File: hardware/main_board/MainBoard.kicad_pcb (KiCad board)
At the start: 2 copper layers, 68 parts, among them J1 5V In, J11 Conn_01x01, J12 GREEN, J13 Conn_01x05, J14 Conn_01x04, J2 9V In, J3 Conn_01x08, J4 Conn_01x08, J5 Conn_01x08, J6 Conn_01x08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

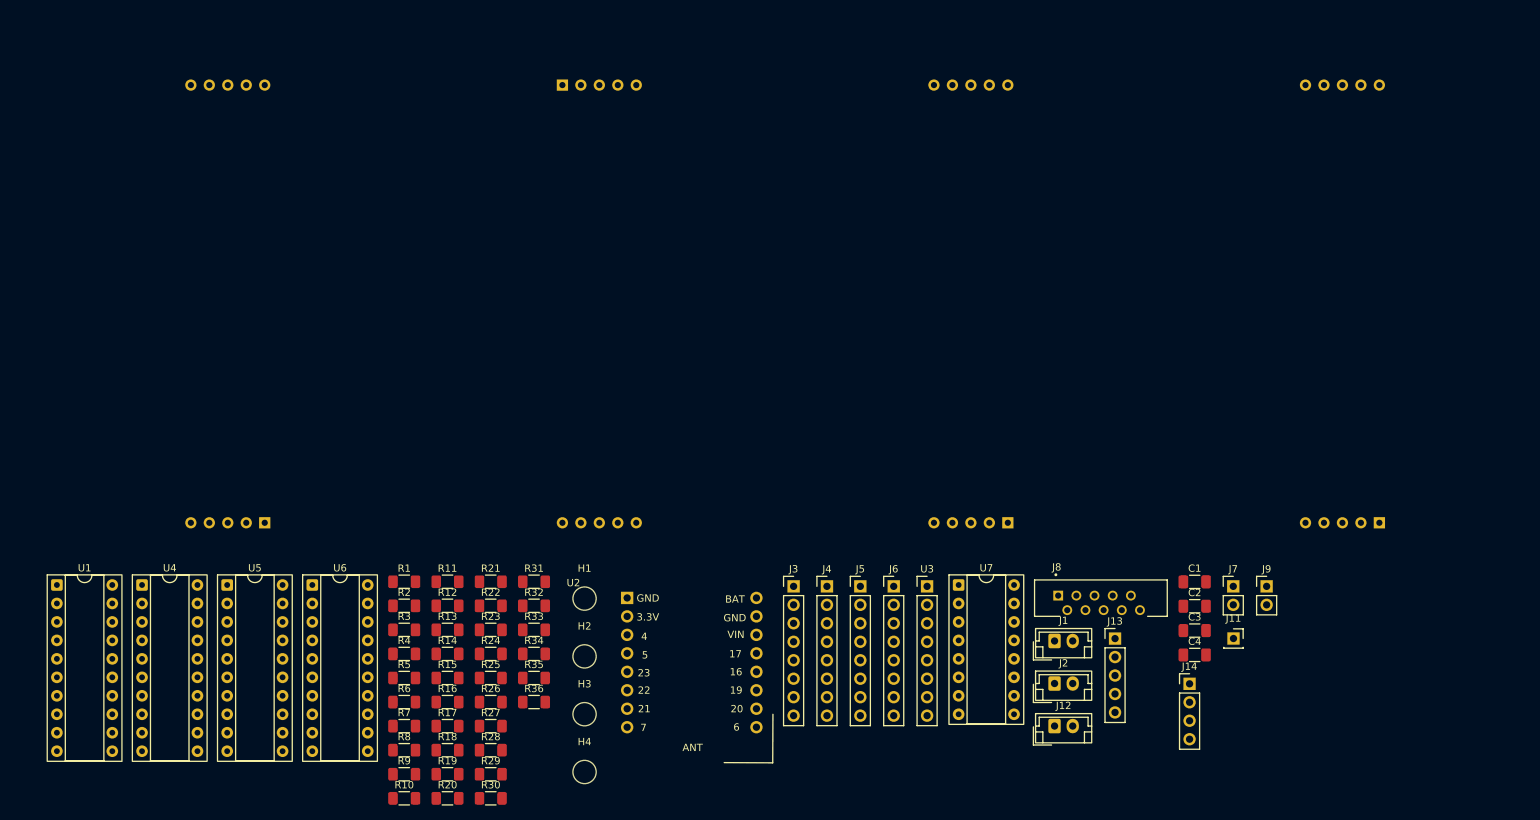
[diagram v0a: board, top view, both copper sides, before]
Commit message: Started 2 layer mainboard, switching to 4 layer
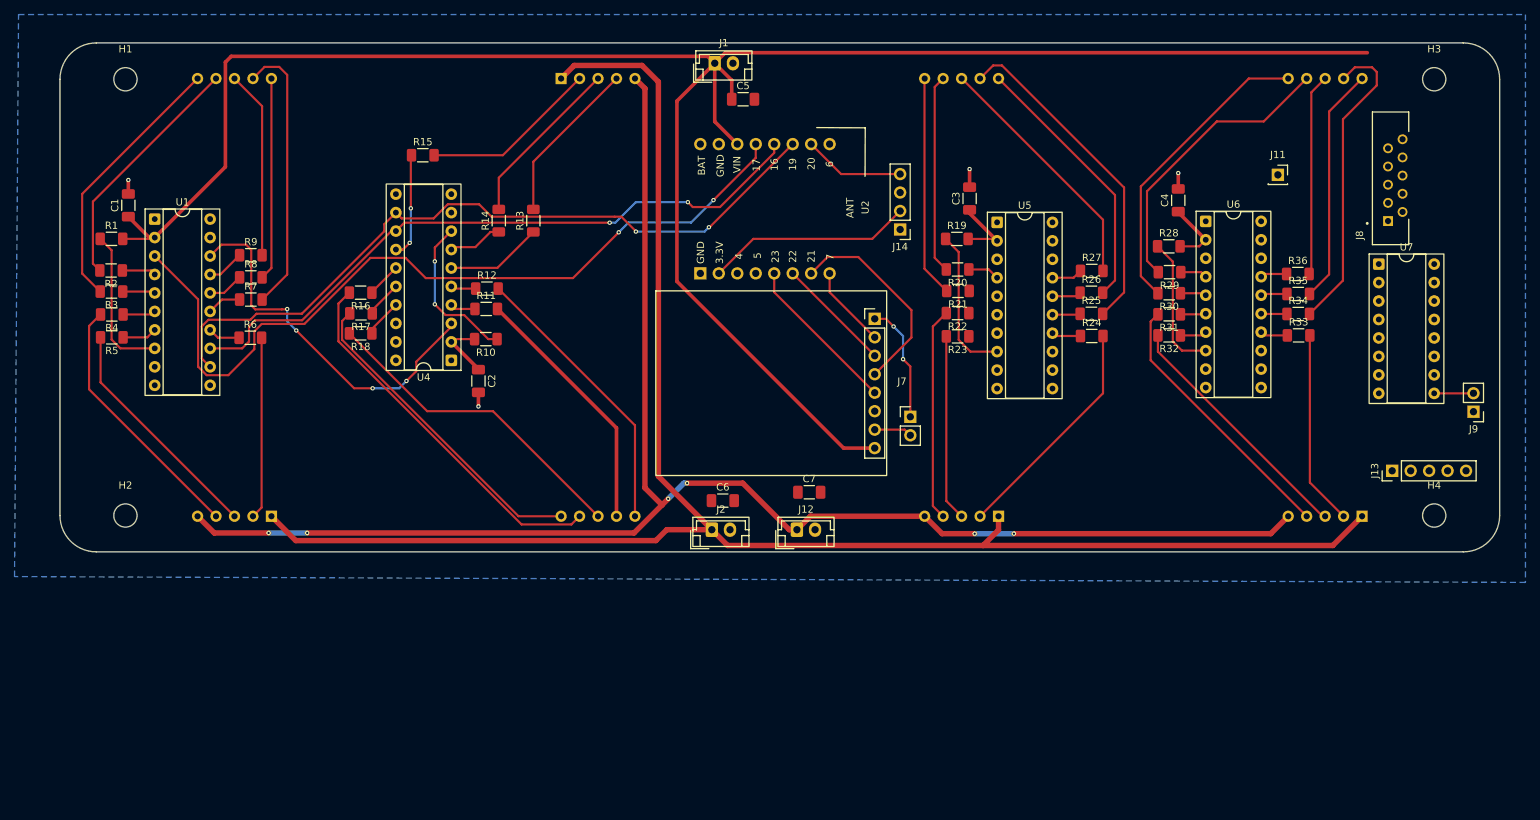
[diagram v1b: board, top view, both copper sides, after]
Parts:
- removed J3, J4, J5, J6: Conn_01x08, Connector_PinHeader_2.54mm:PinHeader_1x08_P2.54mm_Vertical
- added C5: C, Capacitor_SMD:C_1206_3216Metric_Pad1.33x1.80mm_HandSolder, F.Cu at (144.9, 32.8)
- added C6: C, Capacitor_SMD:C_1206_3216Metric_Pad1.33x1.80mm_HandSolder, F.Cu at (142.2, 88.0)
- added C7: C, Capacitor_SMD:C_1206_3216Metric_Pad1.33x1.80mm_HandSolder, F.Cu at (154.1, 86.8)
- U3: footprint Connector_PinHeader_2.54mm:PinHeader_1x08_P2.54mm_Vertical -> GregFootprints:SD Card
- moved C1 155.5 mm to (60.4, 47.3), turned to 90 degrees
- moved H3 145.9 mm to (240.0, 30.0)
- moved U6 132.7 mm to (208.6, 49.5)
- moved H4 122.1 mm to (240.0, 90.0)
- moved R36 120.4 mm to (221.2, 56.8)
- moved R35 117.6 mm to (221.3, 59.5)
- moved U5 117.0 mm to (179.9, 49.7)
- moved R30 116.3 mm to (203.6, 59.4), turned to 180 degrees
- moved R28 116.2 mm to (203.5, 53.0)
- moved R29 116.1 mm to (203.6, 56.5), turned to 180 degrees
- moved R34 115.0 mm to (221.3, 62.3)
- moved R33 112.7 mm to (221.3, 65.2)
- moved R27 103.7 mm to (192.9, 56.4)
- moved C2 103.3 mm to (108.5, 71.5), turned to -90 degrees
- moved R19 101.6 mm to (174.3, 52.0)
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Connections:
- net /DI renamed /MOSI
- net /DO renamed /MISO
- net /SEROUT renamed /SEROUT4
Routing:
- net /5VBus: track 0.00 -> 311.2 mm
- net /9VBus: track 0.00 -> 239.2 mm
- net /GRN: track 0.00 -> 219.4 mm, vias 0 -> 6
- net /SER_In: track 0.00 -> 112.9 mm, vias 0 -> 2
- net /RCLK: track 0.00 -> 102.1 mm, vias 0 -> 2
- net /SRCK: track 0.00 -> 91.7 mm, vias 0 -> 2
- net /SEROUT1: track 0.00 -> 52.2 mm, vias 0 -> 4
- net /2F: track 0.00 -> 51.4 mm
- net /3F: track 0.00 -> 46.1 mm
- net /2DP: track 0.00 -> 45.1 mm
- net /2G: track 0.00 -> 44.2 mm
- net /4F: track 0.00 -> 42.6 mm
- net /4B: track 0.00 -> 42.1 mm
- net /4A: track 0.00 -> 40.2 mm
- net /2B: track 0.00 -> 39.1 mm
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- added copper zone on B.Cu, net GND
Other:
- board outline added: 198 x 70 mm
